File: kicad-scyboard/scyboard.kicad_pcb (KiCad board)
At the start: 2 copper layers, 316 x 95.4 mm, 92 parts, among them U1 Nice_Nano_V2, U2 Nice_Nano_V2

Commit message: Update kicad
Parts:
- D1, D10, D11, D12, D13, D14, D15, D16, D17, D18, D19, D2, D20, D21, D22, D3, D4, D5, D6, D7, D8, D9: footprint ScottoKeebs_Components:Diode_DO-35 -> ScottoKeebs_Components:Diode_SOD-123; moved to B.Cu
- D23, D24, D25, D26, D27, D28, D29, D30, D31, D32, D33, D34, D35, D36, D37, D38, D39, D40, D41, D42, D43, D44: footprint ScottoKeebs_Components:Diode_DO-35 -> ScottoKeebs_Components:Diode_SOD-123
- moved D6 72.1 mm to (140.0, 65.6), turned to 180 degrees
- moved D13 72.0 mm to (50.0, 93.6), turned to 180 degrees
- moved D5 58.8 mm to (122.0, 62.9), turned to 180 degrees
- moved D4 57.5 mm to (104.0, 58.4), turned to 180 degrees
- moved D14 56.8 mm to (68.0, 91.8), turned to 180 degrees
- moved D12 46.8 mm to (140.0, 82.7), turned to 180 degrees
- moved D15 43.8 mm to (86.0, 82.2), turned to 180 degrees
- moved D16 39.5 mm to (104.0, 77.7), turned to 180 degrees
- moved D7 38.1 mm to (50.0, 78.9), turned to 180 degrees
- moved D3 36.9 mm to (86.0, 62.9), turned to 180 degrees
- moved D1 28.4 mm to (50.0, 76.6), turned to 180 degrees
- moved D18 24.9 mm to (140.0, 84.9), turned to 180 degrees
- moved D9 22.6 mm to (86.0, 79.9), turned to 180 degrees
- moved D2 22.3 mm to (68.0, 74.8), turned to 180 degrees
- moved D11 20.6 mm to (122.0, 79.9), turned to 180 degrees
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- renumbered S3 to S1, S11 to S10, S14 to S11, S17 to S12, S1 to S13, S4 to S14, S7 to S15, S10 to S16, S13 to S17, S16 to S18, S6 to S2, S9 to S3, S12 to S4, S15 to S5, S18 to S6, S2 to S7, S5 to S8, S8 to S9
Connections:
- S1 pad 1: Col 3 -> Col 1
- S1 pad 2: Net-(D3-A) -> Net-(D1-A)
- S10 pad 1: Col 5 -> Col 4
- S10 pad 2: Net-(D11-A) -> Net-(D10-A)
- S11 pad 1: Col 2 -> Col 5
- S11 pad 2: Net-(D14-A) -> Net-(D11-A)
- S12 pad 1: Col 5 -> Col 6
- S12 pad 2: Net-(D17-A) -> Net-(D12-A)
- S13 pad 2: Net-(D1-A) -> Net-(D13-A)
- S14 pad 1: Col 4 -> Col 2
- S14 pad 2: Net-(D4-A) -> Net-(D14-A)
- S15 pad 1: Col 1 -> Col 3
- S15 pad 2: Net-(D7-A) -> Net-(D15-A)
- S16 pad 2: Net-(D10-A) -> Net-(D16-A)
- S17 pad 1: Col 1 -> Col 5
- S17 pad 2: Net-(D13-A) -> Net-(D17-A)
- S18 pad 1: Col 4 -> Col 6
- S18 pad 2: Net-(D16-A) -> Net-(D18-A)
- S2 pad 1: Col 6 -> Col 2
- S2 pad 2: Net-(D6-A) -> Net-(D2-A)
- S3 pad 2: Net-(D9-A) -> Net-(D3-A)
- S4 pad 1: Col 6 -> Col 4
- S4 pad 2: Net-(D12-A) -> Net-(D4-A)
- S5 pad 1: Col 3 -> Col 5
- S5 pad 2: Net-(D15-A) -> Net-(D5-A)
- S6 pad 2: Net-(D18-A) -> Net-(D6-A)
- S7 pad 1: Col 2 -> Col 1
- S7 pad 2: Net-(D2-A) -> Net-(D7-A)
- S8 pad 1: Col 5 -> Col 2
- S8 pad 2: Net-(D5-A) -> Net-(D8-A)
- S9 pad 1: Col 2 -> Col 3
- S9 pad 2: Net-(D8-A) -> Net-(D9-A)
- U1 pad 10: Row 2 -> Col 4
- U1 pad 11: Row 3 -> Col 3
- U1 pad 12: Row 4 -> Col 2
- U1 pad 13: Col 6 -> Row 1
- U1 pad 14: Col 5 -> Row 2
- U1 pad 15: Col 4 -> Row 3
- U1 pad 16: Col 3 -> Row 4
- U1 pad 17: Col 2 -> unconnected-(U1-18-Pad17)
- U1 pad 18: Col 1 -> unconnected-(U1-19-Pad18)
- U1 pad 7: unconnected-(U1-4-Pad7) -> Col 1
- U1 pad 8: unconnected-(U1-5-Pad8) -> Col 6
- U1 pad 9: Row 1 -> Col 5
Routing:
- net Col 5: track 0.00 -> 114.0 mm, vias 0 -> 1
- net Col 4: track 0.00 -> 90.3 mm, vias 0 -> 1
- net Col 3: track 0.00 -> 79.0 mm, vias 0 -> 1
- net Col 6: track 0.00 -> 60.1 mm, vias 0 -> 1
- net Col 2: track 0.00 -> 50.7 mm, vias 0 -> 1
- net Col 1: track 0.00 -> 34.0 mm

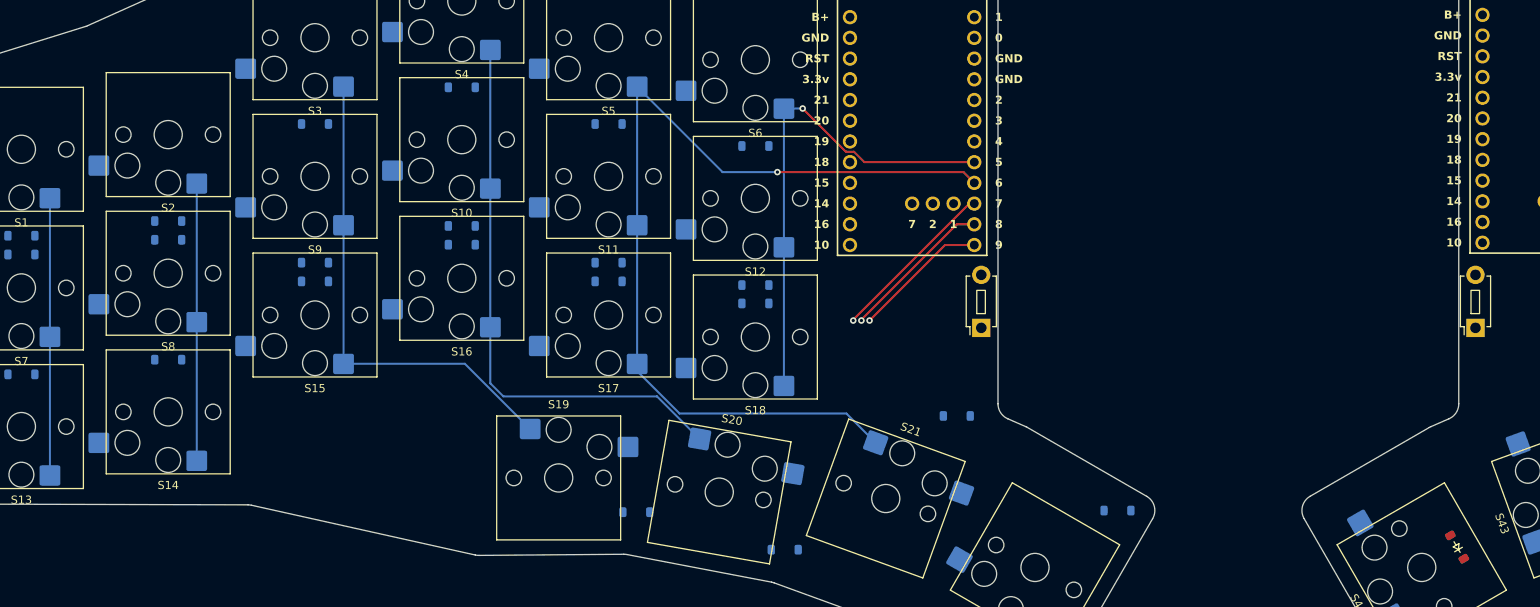
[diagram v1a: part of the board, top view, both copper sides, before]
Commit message: Update kicad
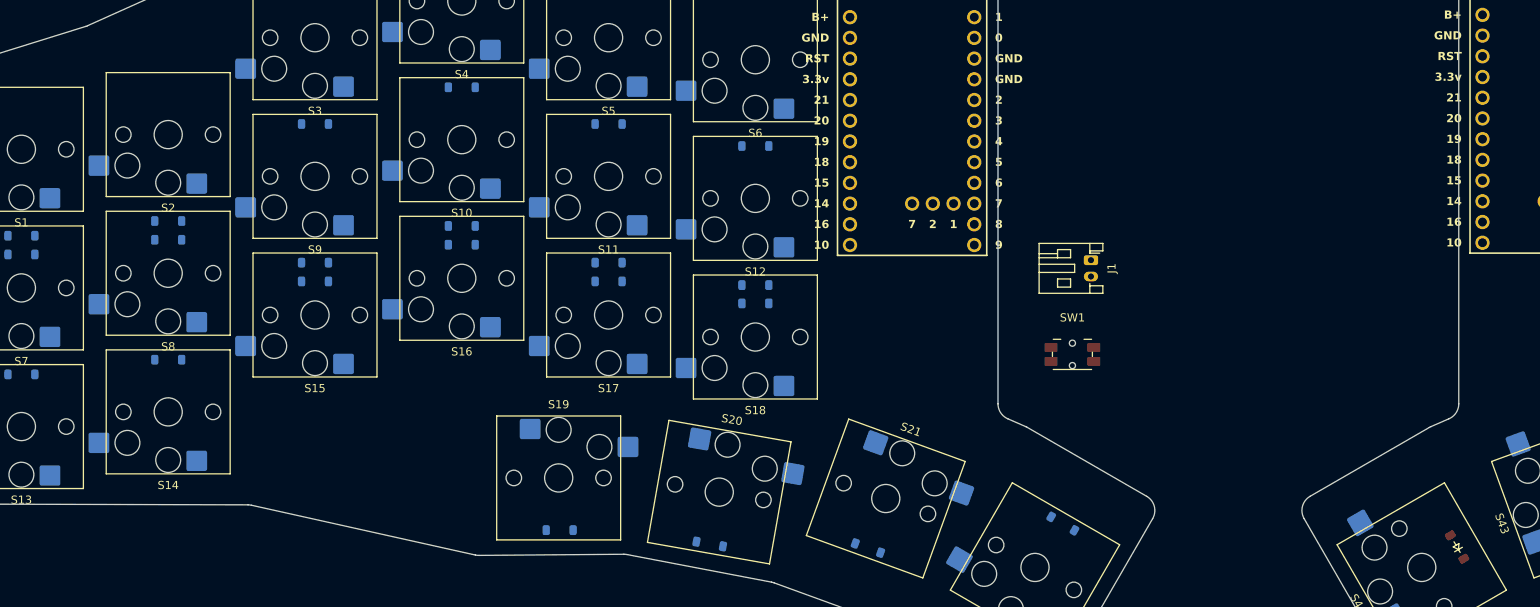
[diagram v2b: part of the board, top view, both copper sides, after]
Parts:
- removed REF** (x2): Button_MJTP1243, ScottoKeebs_Components:Button_MJTP1243
- added J1: JST_L, Connector_JST:JST_PH_S2B-PH-K_1x02_P2.00mm_Horizontal, F.Cu at (181.2, 79.6)
- added SW1: RST_L, Button_Switch_SMD:Panasonic_EVQPUL_EVQPUC, F.Cu at (178.9, 91.2)
- moved D21 19.5 mm to (153.8, 114.9), turned to 160 degrees
- moved D19 9.65 mm to (116.0, 112.7)
- moved D20 9.23 mm to (134.4, 114.4), turned to 170 degrees
- moved D22 6.89 mm to (177.7, 111.9), turned to 150 degrees
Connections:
- U1 pad 1: unconnected-(U1-Pad1) -> Battery -
- U1 pad 22: unconnected-(U1-RST-Pad22) -> RST
- U1 pad 24: unconnected-(U1-B+-Pad24) -> Battery +
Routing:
- net Col 5: track 114.0 -> 0.00 mm, vias 1 -> 0
- net Col 4: track 90.3 -> 0.00 mm, vias 1 -> 0
- net Col 3: track 79.0 -> 0.00 mm, vias 1 -> 0
- net Col 6: track 60.1 -> 0.00 mm, vias 1 -> 0
- net Col 2: track 50.7 -> 0.00 mm, vias 1 -> 0
- net Col 1: track 34.0 -> 0.00 mm

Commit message: Update KiCad
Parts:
- added SW2: PWR_L, Alps_Alpine_Switch_Slide:SW4_SSSS811101_ALPS, F.Cu at (168.1, 91.3)
- added SW3: RST_L, Button_Switch_SMD:Panasonic_EVQPUL_EVQPUC, F.Cu at (237.2, 84.6)
- moved J1 20.3 mm to (161.8, 86.0)
- moved SW1 13.8 mm to (167.8, 82.9), turned to -90 degrees
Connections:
- net Battery + renamed B+L
- net RST renamed RST_L
- J1 pad 1: Battery - -> B-L
- SW1 pad 2: GND -> GND_L1
- U1 pad 1: Battery - -> unconnected-(U1-Pad1)
- U1 pad 21: unconnected-(U1-3.3v-Pad21) -> VCC_L
- U1 pad 23: unconnected-(U1-GND-Pad23) -> B-L
- U1 pad 3: unconnected-(U1-GND-Pad3) -> GND_L1
- U1 pad 4: unconnected-(U1-GND-Pad4) -> GND_L2
- U2 pad 22: unconnected-(U2-RST-Pad22) -> RST_R
- U2 pad 3: unconnected-(U2-GND-Pad3) -> GND_R1

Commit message: Compile
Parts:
- removed J1: JST_L, Connector_JST:JST_PH_S2B-PH-K_1x02_P2.00mm_Horizontal
- removed SW1, SW3: RST_L, Button_Switch_SMD:Panasonic_EVQPUL_EVQPUC
- removed SW2: PWR_L, Alps_Alpine_Switch_Slide:SW4_SSSS811101_ALPS
- removed U1, U2: Nice_Nano_V2, ScottoKeebs_MCU:Nice_Nano_V2_Flipped
- added JST1: , ceoloide:battery_connector_jst_ph_2, F.Cu at (157.1, 89.0)
- added MCU1: , ceoloide:mcu_nice_nano, F.Cu at (159.5, 62.1)
- added PWR1: , ceoloide:power_switch_smd_side, F.Cu at (168.2, 92.9)
- added RST1: , ceoloide:reset_switch_smd_side, F.Cu at (167.9, 83.5)
- D1, D10, D11, D12, D13, D14, D15, D16, D17, D18, D19, D2, D20, D21, D22, D23, D24, D25, D26, D27, D28, D29, D3, D30, D31, D32, D33, D34, D35, D36, D37, D38, D39, D4, D40, D41, D42, D43, D44, D5, D6, D7, D8, D9: value Diode -> (none); footprint ScottoKeebs_Components:Diode_SOD-123 -> ceoloide:diode_tht_sod123
- S1, S10, S11, S12, S13, S14, S15, S16, S17, S18, S19, S2, S20, S21, S22, S3, S4, S5, S6, S7, S8, S9: value Keyswitch -> (none); footprint ScottoKeebs_Hotswap:Hotswap_Choc_V1 -> ceoloide:switch_choc_v1_v2; moved to B.Cu
- S23, S24, S25, S26, S27, S28, S29, S30, S31, S32, S33, S34, S35, S36, S37, S38, S39, S40, S41, S42, S43, S44: value Keyswitch -> (none); footprint ScottoKeebs_Hotswap:Hotswap_Choc_V1 -> ceoloide:switch_choc_v1_v2
- moved S23 296.0 mm to (50.0, 100.0), turned to 180 degrees
- moved S24 296.0 mm to (50.0, 83.0), turned to 180 degrees
- moved S25 296.0 mm to (50.0, 66.0), turned to 180 degrees
- moved D23 288.3 mm to (57.8, 98.5), turned to -90 degrees
- moved D24 288.3 mm to (57.8, 81.5), turned to -90 degrees
- moved D25 288.3 mm to (57.8, 64.5), turned to -90 degrees
- moved S26 260.0 mm to (68.0, 98.2), turned to 180 degrees
- moved S27 260.0 mm to (68.0, 81.2), turned to 180 degrees
- moved S28 260.0 mm to (68.0, 64.2), turned to 180 degrees
- moved D26 252.3 mm to (75.8, 96.7), turned to -90 degrees
- moved D27 252.3 mm to (75.8, 79.7), turned to -90 degrees
- moved D28 252.3 mm to (75.8, 62.7), turned to -90 degrees
- moved S29 224.0 mm to (86.0, 86.3), turned to 180 degrees
- moved S30 224.0 mm to (86.0, 69.3), turned to 180 degrees
- moved S31 224.0 mm to (86.0, 52.3), turned to 180 degrees
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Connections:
- net Net-(D1-A) renamed outer_bottom_B
- net Net-(D10-A) renamed middle_bottom_B
- net Net-(D11-A) renamed middle_home_B
- net Net-(D12-A) renamed middle_top_B
- net Net-(D13-A) renamed index_bottom_B
- net Net-(D14-A) renamed index_home_B
- net Net-(D15-A) renamed index_top_B
- net Net-(D16-A) renamed inner_bottom_B
- net Net-(D17-A) renamed inner_home_B
- net Net-(D18-A) renamed inner_top_B
- net Net-(D19-A) renamed tuck_cluster_B
- net Net-(D2-A) renamed outer_home_B
- net Net-(D20-A) renamed layer_cluster_B
- net Net-(D21-A) renamed space_cluster_B
- net Net-(D22-A) renamed reach_cluster_B
- net Net-(D23-A) renamed outer_bottom_F
- net Net-(D24-A) renamed outer_home_F
- net Net-(D25-A) renamed outer_top_F
- net Net-(D26-A) renamed pinky_bottom_F
- net Net-(D27-A) renamed pinky_home_F
- net Net-(D28-A) renamed pinky_top_F
- net Net-(D29-A) renamed ring_bottom_F
- net Net-(D3-A) renamed outer_top_B
- net Net-(D30-A) renamed ring_home_F
- net Net-(D31-A) renamed ring_top_F
- net Net-(D32-A) renamed middle_bottom_F
- net Net-(D33-A) renamed middle_home_F
- net Net-(D34-A) renamed middle_top_F
- net Net-(D35-A) renamed index_bottom_F
- net Net-(D36-A) renamed index_home_F
- net Net-(D37-A) renamed index_top_F
- net Net-(D38-A) renamed inner_bottom_F
- net Net-(D39-A) renamed inner_home_F
- net Net-(D4-A) renamed pinky_bottom_B
- net Net-(D40-A) renamed inner_top_F
- net Net-(D41-A) renamed tuck_cluster_F
- net Net-(D42-A) renamed layer_cluster_F
- net Net-(D43-A) renamed space_cluster_F
- net Net-(D44-A) renamed reach_cluster_F
- net Net-(D5-A) renamed pinky_home_B
- net Net-(D6-A) renamed pinky_top_B
- net Net-(D7-A) renamed ring_bottom_B
- net Net-(D8-A) renamed ring_home_B
- net Net-(D9-A) renamed ring_top_B
- D1 pad 1: Row 1 -> R2
- D10 pad 1: Row 2 -> R2
- D11 pad 1: Row 2 -> R1
- D12 pad 1: Row 2 -> R0
- D13 pad 1: Row 3 -> R2
- D14 pad 1: Row 3 -> R1
- D15 pad 1: Row 3 -> R0
- D16 pad 1: Row 3 -> R2
- D17 pad 1: Row 3 -> R1
- D18 pad 1: Row 3 -> R0
- D19 pad 1: Row 4 -> R3
- D2 pad 1: Row 1 -> R1
- D20 pad 1: Row 4 -> R3
- D21 pad 1: Row 4 -> R3
- D22 pad 1: Row 4 -> R3
- D23 pad 1: Row 5 -> R2
- D24 pad 1: Row 5 -> R1
- D25 pad 1: Row 5 -> R0
- D26 pad 1: Row 5 -> R2
- D27 pad 1: Row 6 -> R1
- D28 pad 1: Row 6 -> R0
- D29 pad 1: Row 6 -> R2
- D3 pad 1: Row 1 -> R0
- D30 pad 1: Row 6 -> R1
- D31 pad 1: Row 6 -> R0
- D32 pad 1: Row 6 -> R2
- D33 pad 1: Row 7 -> R1
- D34 pad 1: Row 7 -> R0
- D35 pad 1: Row 7 -> R2
- D36 pad 1: Row 7 -> R1
- D37 pad 1: Row 7 -> R0
- D38 pad 1: Row 7 -> R2
- D39 pad 1: Row 8 -> R1
- D4 pad 1: Row 1 -> R2
- D40 pad 1: Row 8 -> R0
- D41 pad 1: Row 8 -> R3
- D42 pad 1: Row 8 -> R3
- D43 pad 1: Row 8 -> R3
- D44 pad 1: Row 8 -> R3
- D5 pad 1: Row 1 -> R1
- D6 pad 1: Row 1 -> R0
- D7 pad 1: Row 2 -> R2
- D8 pad 1: Row 2 -> R1
- D9 pad 1: Row 2 -> R0
- S1 pad 1: Col 1 -> C0
- S10 pad 1: Col 4 -> C3
- S11 pad 1: Col 5 -> C3
- S12 pad 1: Col 6 -> C3
- S13 pad 1: Col 1 -> C4
- S14 pad 1: Col 2 -> C4
- S15 pad 1: Col 3 -> C4
- S16 pad 1: Col 4 -> C5
- S17 pad 1: Col 5 -> C5
- S18 pad 1: Col 6 -> C5
- S19 pad 1: Col 3 -> C2
- S2 pad 1: Col 2 -> C0
- S20 pad 1: Col 4 -> C3
- S21 pad 1: Col 5 -> C4
- S22 pad 1: Col 6 -> C5
- S23 pad 1: Col 7 -> C0
- S24 pad 1: Col 8 -> C0
- S25 pad 1: Col 9 -> C0
- S26 pad 1: Col 10 -> C1
- S27 pad 1: Col 7 -> C1
- S28 pad 1: Col 8 -> C1
- S29 pad 1: Col 9 -> C2
- S3 pad 1: Col 3 -> C0
- S30 pad 1: Col 10 -> C2
- S31 pad 1: Col 11 -> C2
- S32 pad 1: Col 12 -> C3
- S33 pad 1: Col 7 -> C3
- S34 pad 1: Col 8 -> C3
- S35 pad 1: Col 9 -> C4
- S36 pad 1: Col 10 -> C4
- S37 pad 1: Col 11 -> C4
- S38 pad 1: Col 12 -> C5
- S39 pad 1: Col 7 -> C5
- S4 pad 1: Col 4 -> C1
- S40 pad 1: Col 8 -> C5
- S41 pad 1: Col 9 -> C2
- S42 pad 1: Col 10 -> C3
- S43 pad 1: Col 11 -> C4
- S44 pad 1: Col 12 -> C5
- S5 pad 1: Col 5 -> C1
- S6 pad 1: Col 6 -> C1
- S7 pad 1: Col 1 -> C2
- S8 pad 1: Col 2 -> C2
- S9 pad 1: Col 3 -> C2
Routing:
- net GND: track 0.00 -> 28.9 mm
- net P10: track 0.00 -> 9.64 mm
- net RST: track 0.00 -> 9.64 mm
- net RAW: track 0.00 -> 9.64 mm
- net C5: track 0.00 -> 9.64 mm
- net C2: track 0.00 -> 9.64 mm
- net C1: track 0.00 -> 9.64 mm
- net VCC: track 0.00 -> 9.64 mm
- net P16: track 0.00 -> 9.64 mm
- net C4: track 0.00 -> 9.64 mm
- net C3: track 0.00 -> 9.64 mm
- net C0: track 0.00 -> 9.64 mm
- net R0: track 0.00 -> 9.63 mm
- net LED: track 0.00 -> 9.63 mm
- net SDA: track 0.00 -> 9.63 mm
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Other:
- board size 316 x 95.4 mm -> 149 x 95.4 mm

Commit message: Compile
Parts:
- S1, S10, S11, S12, S13, S14, S15, S16, S17, S18, S19, S2, S20, S21, S4, S5, S6, S7, S8, S9: footprint ceoloide:switch_choc_v1_v2 -> custom:custom_switch_choc_v1_v2
- S22: footprint ceoloide:switch_choc_v1_v2 -> custom:custom_switch_choc_v1_v2_2.00u

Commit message: Compile
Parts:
- S1, S10, S11, S12, S13, S14, S15, S16, S17, S18, S19, S2, S20, S21, S4, S5, S6, S7, S8, S9: footprint custom:custom_switch_choc_v1_v2 -> ceoloide:switch_choc_v1_v2
- S22: footprint custom:custom_switch_choc_v1_v2_2.00u -> ceoloide:switch_choc_v1_v2
- moved JST1 4.90 mm to (161.9, 89.0)
- turned RST1 to 0 degrees
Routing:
- net (no net): track 0.00 -> 333.1 mm
- net GND: track 28.9 -> 0.00 mm
- net P10: track 9.64 -> 0.00 mm
- net RST: track 9.64 -> 0.00 mm
- net RAW: track 9.64 -> 0.00 mm
- net C5: track 9.64 -> 0.00 mm
- net C2: track 9.64 -> 0.00 mm
- net C1: track 9.64 -> 0.00 mm
- net VCC: track 9.64 -> 0.00 mm
- net P16: track 9.64 -> 0.00 mm
- net C4: track 9.64 -> 0.00 mm
- net C3: track 9.64 -> 0.00 mm
- net C0: track 9.64 -> 0.00 mm
- net R0: track 9.63 -> 0.00 mm
- net LED: track 9.63 -> 0.00 mm
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
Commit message: Update KiCad
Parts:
- moved D44 6.06 mm to (165.7, 125.6), turned to -214 degrees
- moved S22 5.59 mm to (168.8, 118.3), turned to 56 degrees
- moved S44 5.59 mm to (168.8, 118.3), turned to 56 degrees
- moved D22 5.28 mm to (174.4, 112.7), turned to -214 degrees
- moved D43 4.36 mm to (150.4, 116.1), turned to -207 degrees
- moved D19 4.14 mm to (105.2, 101.8)
- moved D41 4.14 mm to (120.8, 101.8)
- moved S19 4.14 mm to (113.0, 103.3)
- moved S41 4.14 mm to (113.0, 103.3)
- moved D20 3.72 mm to (125.3, 102.8), turned to -105 degrees
- moved S20 3.59 mm to (132.4, 106.3), turned to 165 degrees
- moved S42 3.59 mm to (132.4, 106.3), turned to 165 degrees
- moved S21 3.40 mm to (152.6, 108.5), turned to 63 degrees
- moved S43 3.40 mm to (152.6, 108.5), turned to 63 degrees
- moved D42 3.32 mm to (140.3, 106.8), turned to -105 degrees
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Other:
- board size 149 x 95.4 mm -> 143.9 x 96.5 mm

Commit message: Update KiCad
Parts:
- turned RST1 to -90 degrees
- turned JST1 to -90 degrees
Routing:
- net (no net): track 333.1 -> 0.00 mm
- net GND: track 0.00 -> 28.9 mm
- net P10: track 0.00 -> 9.64 mm
- net RST: track 0.00 -> 9.64 mm
- net RAW: track 0.00 -> 9.64 mm
- net C5: track 0.00 -> 9.64 mm
- net C2: track 0.00 -> 9.64 mm
- net C1: track 0.00 -> 9.64 mm
- net VCC: track 0.00 -> 9.64 mm
- net P16: track 0.00 -> 9.64 mm
- net C4: track 0.00 -> 9.64 mm
- net C3: track 0.00 -> 9.64 mm
- net C0: track 0.00 -> 9.64 mm
- net R0: track 0.00 -> 9.63 mm
- net LED: track 0.00 -> 9.63 mm
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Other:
- board size 143.9 x 96.5 mm -> 144 x 96.5 mm
